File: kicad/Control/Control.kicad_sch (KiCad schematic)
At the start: 66 parts, among them J1 Control Connector, J2 Data Connector, U1 27C64, U10 74LS377, U11 74LS253, U12 74LS253, U13 74LS253, U14 74LS253, U15 74LS253, U16 74LS253, U17 74LS253, U18 74LS257, U19 74LS377, U2 27C64, U20 74LS377, U21 74LS377, U22 74LS138, U23 74LS32, U24 74LS08, U25 74LS86, U26 74LS74, U3 27C64, U4 27C64, U5 27C64, U6 74LS273, U7 74LS377, U8 74LS377, U9 74LS377

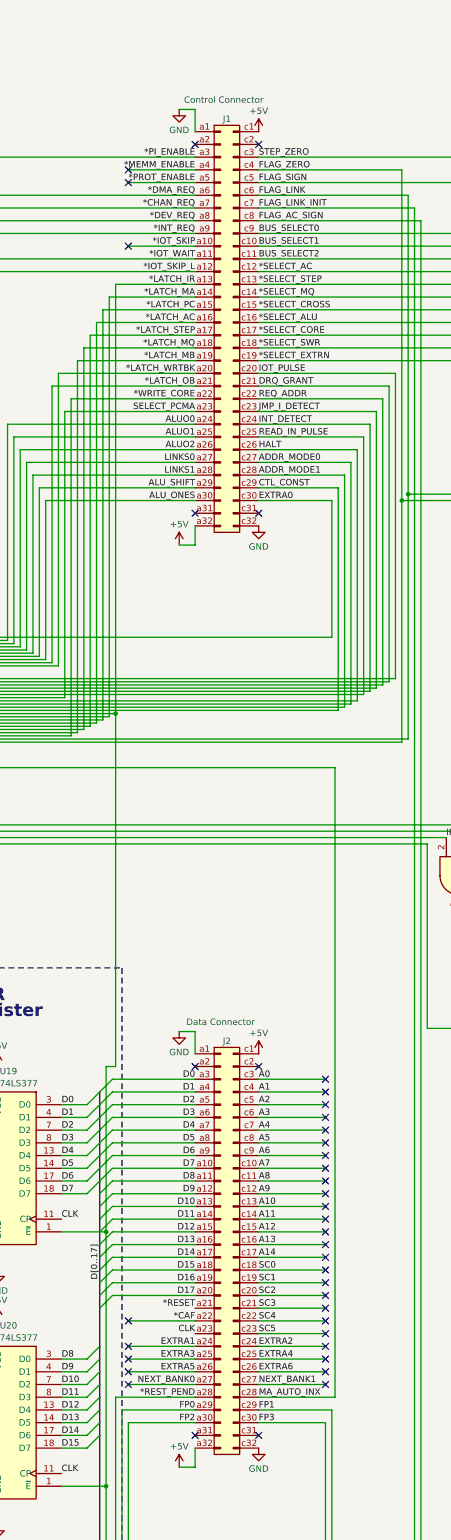
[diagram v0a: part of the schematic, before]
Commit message: Start work on backplane and fix connectors
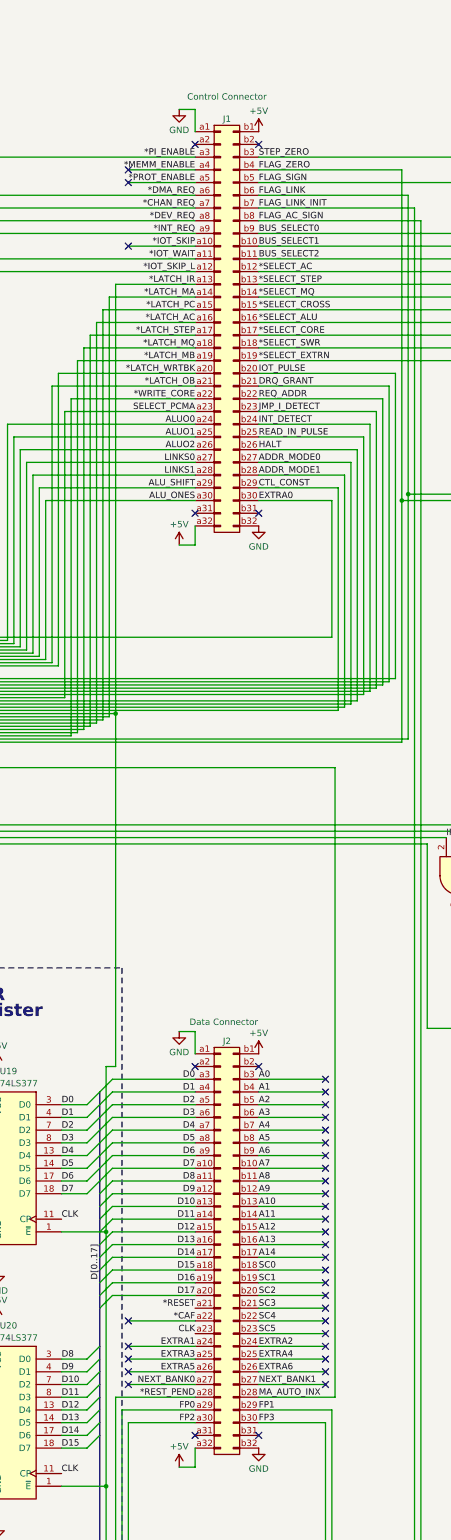
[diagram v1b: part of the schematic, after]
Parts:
- removed J1: Control Connector, symbol Connector:DIN41612_02x32_AC
- removed J2: Data Connector, symbol Connector:DIN41612_02x32_AC
- added J1: Control Connector, Connector_DIN:DIN41612_B_2x32_Male_Horizontal_THT, symbol Connector:DIN41612_02x32_AB
- added J2: Data Connector, Connector_DIN:DIN41612_B_2x32_Male_Horizontal_THT, symbol Connector:DIN41612_02x32_AB
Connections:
- net *CAF: now also J2.a22 (Pin_a22)
- net *CHAN_REQ: now also J1.a7 (Pin_a7)
- net *DEV_REQ: now also J1.a8 (Pin_a8)
- net *DMA_REQ: now also J1.a6 (Pin_a6)
- net *INT_REQ: now also J1.a9 (Pin_a9)
- net *IOT_SKIP: now also J1.a10 (Pin_a10)
- net *IOT_SKIP_L: now also J1.a12 (Pin_a12)
- net *IOT_WAIT: now also J1.a11 (Pin_a11)
- net *LATCH_AC: now also J1.a16 (Pin_a16)
- net *LATCH_IR: now also J1.a13 (Pin_a13)
- net *LATCH_MA: now also J1.a14 (Pin_a14)
- net *LATCH_MB: now also J1.a19 (Pin_a19)
- net *LATCH_MQ: now also J1.a18 (Pin_a18)
- net *LATCH_OB: now also J1.a21 (Pin_a21)
- net *LATCH_PC: now also J1.a15 (Pin_a15)
- net *LATCH_STEP: now also J1.a17 (Pin_a17)
- net *LATCH_WRTBK: now also J1.a20 (Pin_a20)
- net *MEMM_ENABLE: now also J1.a4 (Pin_a4)
- net *PI_ENABLE: now also J1.a3 (Pin_a3)
- net *PROT_ENABLE: now also J1.a5 (Pin_a5)
- net *RESET: now also J2.a21 (Pin_a21)
- net *REST_PEND: now also J2.a28 (Pin_a28)
- net *SELECT_AC: now also J1.b12 (Pin_b12)
- net *SELECT_ALU: now also J1.b16 (Pin_b16)
- net *SELECT_CORE: now also J1.b17 (Pin_b17)
- net *SELECT_CROSS: now also J1.b15 (Pin_b15)
- net *SELECT_EXTRN: now also J1.b19 (Pin_b19)
- net *SELECT_MQ: now also J1.b14 (Pin_b14)
- net *SELECT_STEP: now also J1.b13 (Pin_b13)
- net *SELECT_SWR: now also J1.b18 (Pin_b18)
- net *WRITE_CORE: now also J1.a22 (Pin_a22)
- net +5V: now also J1.a32 (Pin_a32), J1.b1 (Pin_b1), J2.a32 (Pin_a32), J2.b1 (Pin_b1)
- net A0: now also J2.b3 (Pin_b3)
- net A1: now also J2.b4 (Pin_b4)
- net A10: now also J2.b13 (Pin_b13)
- net A11: now also J2.b14 (Pin_b14)
- net A12: now also J2.b15 (Pin_b15)
- net A13: now also J2.b16 (Pin_b16)
- net A14: now also J2.b17 (Pin_b17)
- net A2: now also J2.b5 (Pin_b5)
- net A3: now also J2.b6 (Pin_b6)
- net A4: now also J2.b7 (Pin_b7)
- net A5: now also J2.b8 (Pin_b8)
- net A6: now also J2.b9 (Pin_b9)
- net A7: now also J2.b10 (Pin_b10)
- net A8: now also J2.b11 (Pin_b11)
- net A9: now also J2.b12 (Pin_b12)
- net ADDR_MODE0: now also J1.b27 (Pin_b27)
- net ADDR_MODE1: now also J1.b28 (Pin_b28)
- net ALUO0: now also J1.a24 (Pin_a24)
- net ALUO1: now also J1.a25 (Pin_a25)
- net ALUO2: now also J1.a26 (Pin_a26)
- net ALU_ONES: now also J1.a30 (Pin_a30)
- net ALU_SHIFT: now also J1.a29 (Pin_a29)
- net BUS_SELECT0: now also J1.b9 (Pin_b9)
- net BUS_SELECT1: now also J1.b10 (Pin_b10)
- net BUS_SELECT2: now also J1.b11 (Pin_b11)
- net CLK: now also J2.a23 (Pin_a23)
- net CTL_CONST: now also J1.b29 (Pin_b29)
- net D0: now also J2.a3 (Pin_a3)
- net D1: now also J2.a4 (Pin_a4)
- net D10: now also J2.a13 (Pin_a13)
- net D11: now also J2.a14 (Pin_a14)
- net D12: now also J2.a15 (Pin_a15)
- net D13: now also J2.a16 (Pin_a16)
- net D14: now also J2.a17 (Pin_a17)
- net D15: now also J2.a18 (Pin_a18)
- net D16: now also J2.a19 (Pin_a19)
- net D17: now also J2.a20 (Pin_a20)
- net D2: now also J2.a5 (Pin_a5)
- net D3: now also J2.a6 (Pin_a6)
- net D4: now also J2.a7 (Pin_a7)
- net D5: now also J2.a8 (Pin_a8)
- net D6: now also J2.a9 (Pin_a9)
- net D7: now also J2.a10 (Pin_a10)
- net D8: now also J2.a11 (Pin_a11)
- net D9: now also J2.a12 (Pin_a12)
- net DRQ_GRANT: now also J1.b21 (Pin_b21)
- net EXTRA0: now also J1.b30 (Pin_b30)
- net EXTRA1: now also J2.a24 (Pin_a24)
- net EXTRA2: now also J2.b24 (Pin_b24)
- net EXTRA3: now also J2.a25 (Pin_a25)
- net EXTRA4: now also J2.b25 (Pin_b25)
- net EXTRA5: now also J2.a26 (Pin_a26)
- net EXTRA6: now also J2.b26 (Pin_b26)
- net FLAG_AC_SIGN: now also J1.b8 (Pin_b8)
- net FLAG_LINK: now also J1.b6 (Pin_b6)
- net FLAG_LINK_INIT: now also J1.b7 (Pin_b7)
- net FLAG_SIGN: now also J1.b5 (Pin_b5)
- net FLAG_ZERO: now also J1.b4 (Pin_b4)
- net FP0: now also J2.a29 (Pin_a29)
- net FP1: now also J2.b29 (Pin_b29)
- net FP2: now also J2.a30 (Pin_a30)
- net FP3: now also J2.b30 (Pin_b30)
- net GND: now also J1.a1 (Pin_a1), J1.b32 (Pin_b32), J2.a1 (Pin_a1), J2.b32 (Pin_b32)
- net HALT: now also J1.b26 (Pin_b26)
- net INT_DETECT: now also J1.b24 (Pin_b24)
- net IOT_PULSE: now also J1.b20 (Pin_b20)
- net JMP_I_DETECT: now also J1.b23 (Pin_b23)
- net LINKS0: now also J1.a27 (Pin_a27)
- net LINKS1: now also J1.a28 (Pin_a28)
- net MA_AUTO_INX: now also J2.b28 (Pin_b28)
- net NEXT_BANK0: now also J2.a27 (Pin_a27)
- net NEXT_BANK1: now also J2.b27 (Pin_b27)
- net READ_IN_PULSE: now also J1.b25 (Pin_b25)
- net REQ_ADDR: now also J1.b22 (Pin_b22)
- net SC0: now also J2.b18 (Pin_b18)
- net SC1: now also J2.b19 (Pin_b19)
- net SC2: now also J2.b20 (Pin_b20)
- net SC3: now also J2.b21 (Pin_b21)
- net SC4: now also J2.b22 (Pin_b22)
- net SC5: now also J2.b23 (Pin_b23)
- net SELECT_PCMA: now also J1.a23 (Pin_a23)
- net STEP_ZERO: now also J1.b3 (Pin_b3)
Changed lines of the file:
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@@
     (effects (font (size 1.27 1.27)) (justify right bottom))
   )
-  (symbol (lib_id "Connector:DIN41612_02x32_AC") (at 476.885 273.685 0) (unit 1)
-    (in_bom yes) (on_board yes) (dnp no)
-    (property "Reference" "J2" (at 478.155 233.045 0)
-      (effects (font (size 1.27 1.27)))
-    )
-    (property "Value" "Data Connector" (at 476.885 229.235 0)
-      (effects (font (size 1.27 1.27)))
-    )
-    (property "Footprint" "" (at 476.885 273.685 0)
-      (effects (font (size 1.27 1.27)) hide)
-    )
-    (property "Datasheet" "~" (at 476.885 273.685 0)
-      (effects (font (size 1.27 1.27)) hide)
-    )
-    (pin "a1")
-    (pin "a10")
-    (pin "a11")
-    (pin "a12")
-    (pin "a13")
-    (pin "a14")
-    (pin "a15")
-    (pin "a16")
-    (pin "a17")
-    (pin "a18")
-    (pin "a19")
-    (pin "a2")
-    (pin "a20")
-    (pin "a21")
-    (pin "a22")
-    (pin "a23")
-    (pin "a24")
-    (pin "a25")
-    (pin "a26")
-    (pin "a27")
-    (pin "a28")
-    (pin "a29")
-    (pin "a3")
-    (pin "a30")
-    (pin "a31")
-    (pin "a32")
-    (pin "a4")
-    (pin "a5")
-    (pin "a6")
-    (pin "a7")
-    (pin "a8")
-    (pin "a9")
-    (pin "c1")
-    (pin "c10")
-    (pin "c11")
-    (pin "c12")
-    (pin "c13")
-    (pin "c14")
-    (pin "c15")
-    (pin "c16")
-    (pin "c17")
-    (pin "c18")
-    (pin "c19")
-    (pin "c2")
-    (pin "c20")
-    (pin "c21")
-    (pin "c22")
-    (pin "c23")
-    (pin "c24")
-    (pin "c25")
-    (pin "c26")
-    (pin "c27")
-    (pin "c28")
-    (pin "c29")
-    (pin "c3")
-    (pin "c30")
-    (pin "c31")
-    (pin "c32")
-    (pin "c4")
-    (pin "c5")
-    (pin "c6")
-    (pin "c7")
-    (pin "c8")
-    (pin "c9")
-    (instances
-      (project "Control"
-        (path "/9aceca4c-796d-4c9d-8044-fc5cfdda262d"
-          (reference "J2") (unit 1)
-        )
-      )
-      (project "ALU"
-        (path "/b26dce39-0c19-4808-8ddd-74847f21ad13"
-          (reference "J2") (unit 1)
-        )
-      )
-    )
-  )
   (symbol (lib_id "74xx:74LS74") (at 114.3 385.445 0) (unit 3)
     (in_bom yes) (on_board yes) (dnp no) (fields_autoplaced)
@@
     )
   )
+  (symbol (lib_id "Connector:DIN41612_02x32_AB") (at 476.885 273.685 0) (unit 1)
+    (in_bom yes) (on_board yes) (dnp no)
+    (property "Reference" "J2" (at 478.155 233.045 0)
+      (effects (font (size 1.27 1.27)))
+    )
+    (property "Value" "Data Connector" (at 477.52 229.235 0)
+      (effects (font (size 1.27 1.27)))
+    )
+    (property "Footprint" "Connector_DIN:DIN41612_B_2x32_Male_Horizontal_THT" (at 476.885 273.685 0)
+      (effects (font (size 1.27 1.27)) hide)
+    )
+    (property "Datasheet" "~" (at 476.885 273.685 0)
+      (effects (font (size 1.27 1.27)) hide)
+    )
+    (pin "a1")
+    (pin "a10")
+    (pin "a11")
+    (pin "a12")
+    (pin "a13")
+    (pin "a14")
+    (pin "a15")
+    (pin "a16")
+    (pin "a17")
+    (pin "a18")
+    (pin "a19")
+    (pin "a2")
+    (pin "a20")
+    (pin "a21")
+    (pin "a22")
+    (pin "a23")
+    (pin "a24")
+    (pin "a25")
+    (pin "a26")
+    (pin "a27")
+    (pin "a28")
+    (pin "a29")
+    (pin "a3")
+    (pin "a30")
+    (pin "a31")
+    (pin "a32")
+    (pin "a4")
+    (pin "a5")
+    (pin "a6")
+    (pin "a7")
+    (pin "a8")
+    (pin "a9")
+    (pin "b1")
+    (pin "b10")
+    (pin "b11")
+    (pin "b12")
+    (pin "b13")
+    (pin "b14")
+    (pin "b15")
+    (pin "b16")
+    (pin "b17")
+    (pin "b18")
+    (pin "b19")
+    (pin "b2")
+    (pin "b20")
+    (pin "b21")
+    (pin "b22")
+    (pin "b23")
+    (pin "b24")
+    (pin "b25")
+    (pin "b26")
+    (pin "b27")
+    (pin "b28")
+    (pin "b29")
+    (pin "b3")
+    (pin "b30")
+    (pin "b31")
+    (pin "b32")
+    (pin "b4")
+    (pin "b5")
+    (pin "b6")
+    (pin "b7")
+    (pin "b8")
+    (pin "b9")
+    (instances
+      (project "Control"
+        (path "/9aceca4c-796d-4c9d-8044-fc5cfdda262d"
+          (reference "J2") (unit 1)
+        )
+      )
+      (project "ALU"
+        (path "/b26dce39-0c19-4808-8ddd-74847f21ad13"
+          (reference "J2") (unit 1)
+        )
+      )
+    )
+  )
   (symbol (lib_id "74xx:74LS08") (at 39.37 357.505 0) (unit 4)
     (in_bom yes) (on_board yes) (dnp no) (fields_autoplaced)
@@
     )
   )
-  (symbol (lib_id "Connector:DIN41612_02x32_AC") (at 476.885 89.535 0) (unit 1)
-    (in_bom yes) (on_board yes) (dnp no)
-    (property "Reference" "J1" (at 478.155 48.895 0)
-      (effects (font (size 1.27 1.27)))
-    )
-    (property "Value" "Control Connector" (at 477.52 45.085 0)
-      (effects (font (size 1.27 1.27)))
-    )
-    (property "Footprint" "" (at 476.885 89.535 0)
-      (effects (font (size 1.27 1.27)) hide)
-    )
-    (property "Datasheet" "~" (at 476.885 89.535 0)
-      (effects (font (size 1.27 1.27)) hide)
-    )
-    (pin "a1")
-    (pin "a10")
-    (pin "a11")
-    (pin "a12")
-    (pin "a13")
-    (pin "a14")
-    (pin "a15")
-    (pin "a16")
-    (pin "a17")
-    (pin "a18")
-    (pin "a19")
-    (pin "a2")
-    (pin "a20")
-    (pin "a21")
-    (pin "a22")
-    (pin "a23")
-    (pin "a24")
-    (pin "a25")
-    (pin "a26")
-    (pin "a27")
-    (pin "a28")
-    (pin "a29")
-    (pin "a3")
-    (pin "a30")
-    (pin "a31")
-    (pin "a32")
-    (pin "a4")
-    (pin "a5")
-    (pin "a6")
-    (pin "a7")
-    (pin "a8")
-    (pin "a9")
-    (pin "c1")
-    (pin "c10")
-    (pin "c11")
-    (pin "c12")
-    (pin "c13")
-    (pin "c14")
-    (pin "c15")
-    (pin "c16")
-    (pin "c17")
-    (pin "c18")
-    (pin "c19")
-    (pin "c2")
-    (pin "c20")
-    (pin "c21")
-    (pin "c22")
-    (pin "c23")
-    (pin "c24")
-    (pin "c25")
-    (pin "c26")
-    (pin "c27")
-    (pin "c28")
-    (pin "c29")
-    (pin "c3")
-    (pin "c30")
-    (pin "c31")
-    (pin "c32")
-    (pin "c4")
-    (pin "c5")
-    (pin "c6")
-    (pin "c7")
-    (pin "c8")
-    (pin "c9")
-    (instances
-      (project "Control"
-        (path "/9aceca4c-796d-4c9d-8044-fc5cfdda262d"
-          (reference "J1") (unit 1)
-        )
-      )
-      (project "ALU"
-        (path "/b26dce39-0c19-4808-8ddd-74847f21ad13"
-          (reference "J1") (unit 1)
-        )
-      )
-    )
-  )
   (symbol (lib_id "power:+5V") (at 297.815 293.37 0) (unit 1)
     (in_bom yes) (on_board yes) (dnp no) (fields_autoplaced)
@@
         )
       )
+    )
+  )
+  (symbol (lib_id "Connector:DIN41612_02x32_AB") (at 476.885 89.535 0) (unit 1)
+    (in_bom yes) (on_board yes) (dnp no)
+    (property "Reference" "J1" (at 478.155 48.895 0)
+      (effects (font (size 1.27 1.27)))
+    )
+    (property "Value" "Control Connector" (at 478.155 44.45 0)
+      (effects (font (size 1.27 1.27)))
+    )
+    (property "Footprint" "Connector_DIN:DIN41612_B_2x32_Male_Horizontal_THT" (at 476.885 89.535 0)
+      (effects (font (size 1.27 1.27)) hide)
+    )
+    (property "Datasheet" "~" (at 476.885 89.535 0)
+      (effects (font (size 1.27 1.27)) hide)
+    )
+    (pin "a1")
+    (pin "a10")
+    (pin "a11")
+    (pin "a12")
+    (pin "a13")
+    (pin "a14")
+    (pin "a15")
+    (pin "a16")
+    (pin "a17")
+    (pin "a18")
+    (pin "a19")
+    (pin "a2")
+    (pin "a20")
+    (pin "a21")
+    (pin "a22")
+    (pin "a23")
+    (pin "a24")
+    (pin "a25")
+    (pin "a26")
+    (pin "a27")
+    (pin "a28")
+    (pin "a29")
+    (pin "a3")
+    (pin "a30")
+    (pin "a31")
+    (pin "a32")
+    (pin "a4")
+    (pin "a5")
+    (pin "a6")
+    (pin "a7")
+    (pin "a8")
+    (pin "a9")
+    (pin "b1")
+    (pin "b10")
+    (pin "b11")
+    (pin "b12")
+    (pin "b13")
+    (pin "b14")
+    (pin "b15")
+    (pin "b16")
+    (pin "b17")
+    (pin "b18")
+    (pin "b19")
+    (pin "b2")
+    (pin "b20")
+    (pin "b21")
+    (pin "b22")
+    (pin "b23")
+    (pin "b24")
+    (pin "b25")
+    (pin "b26")
+    (pin "b27")
+    (pin "b28")
+    (pin "b29")
+    (pin "b3")
+    (pin "b30")
+    (pin "b31")
+    (pin "b32")
+    (pin "b4")
+    (pin "b5")
+    (pin "b6")
+    (pin "b7")
+    (pin "b8")
+    (pin "b9")
+    (instances
+      (project "Control"
+        (path "/9aceca4c-796d-4c9d-8044-fc5cfdda262d"
+          (reference "J1") (unit 1)
+        )
+      )
+      (project "ALU"
+        (path "/b26dce39-0c19-4808-8ddd-74847f21ad13"
+          (reference "J1") (unit 1)
+        )
+      )

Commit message: Update backplane pin logic levels
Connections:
- net DRQ_GRANT renamed *DRQ_GRANT
- net INT_DETECT renamed *INT_DETECT
- net IOT_PULSE renamed *IOT_PULSE
- net JMP_I_DETECT renamed *JMP_I_DETECT
- net READ_IN_PULSE renamed *READ_IN_PULSE
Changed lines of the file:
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@@
     (effects (font (size 1.27 1.27)) (justify right bottom))
   )
-  (label "INT_DETECT" (at 257.175 124.46 0) (fields_autoplaced)
+  (label "*INT_DETECT" (at 257.175 124.46 0) (fields_autoplaced)
     (effects (font (size 1.27 1.27)) (justify left bottom))
   )
@@
     (effects (font (size 1.27 1.27)) (justify left bottom))
   )
-  (label "JMP_I_DETECT" (at 484.505 107.315 0) (fields_autoplaced)
+  (label "*JMP_I_DETECT" (at 484.505 107.315 0) (fields_autoplaced)
     (effects (font (size 1.27 1.27)) (justify left bottom))
   )
@@
     (effects (font (size 1.27 1.27)) (justify right bottom))
   )
-  (label "IOT_PULSE" (at 257.175 114.3 0) (fields_autoplaced)
+  (label "*IOT_PULSE" (at 257.175 114.3 0) (fields_autoplaced)
     (effects (font (size 1.27 1.27)) (justify left bottom))
   )
@@
     (effects (font (size 1.27 1.27)) (justify right bottom))
   )
-  (label "IOT_PULSE" (at 484.505 99.695 0) (fields_autoplaced)
+  (label "*IOT_PULSE" (at 484.505 99.695 0) (fields_autoplaced)
     (effects (font (size 1.27 1.27)) (justify left bottom))
   )
@@
     (effects (font (size 1.27 1.27)) (justify right bottom))
   )
-  (label "JMP_I_DETECT" (at 257.175 121.92 0) (fields_autoplaced)
+  (label "*JMP_I_DETECT" (at 257.175 121.92 0) (fields_autoplaced)
     (effects (font (size 1.27 1.27)) (justify left bottom))
   )
@@
     (effects (font (size 1.27 1.27)) (justify left bottom))
   )
-  (label "DRQ_GRANT" (at 257.175 116.84 0) (fields_autoplaced)
+  (label "*DRQ_GRANT" (at 257.175 116.84 0) (fields_autoplaced)
     (effects (font (size 1.27 1.27)) (justify left bottom))
   )
@@
     (effects (font (size 1.27 1.27)) (justify right bottom))
   )
-  (label "READ_IN_PULSE" (at 257.175 127 0) (fields_autoplaced)
+  (label "*READ_IN_PULSE" (at 257.175 127 0) (fields_autoplaced)
     (effects (font (size 1.27 1.27)) (justify left bottom))
   )
@@
     (effects (font (size 1.27 1.27)) (justify right bottom))
   )
-  (label "READ_IN_PULSE" (at 484.505 112.395 0) (fields_autoplaced)
+  (label "*READ_IN_PULSE" (at 484.505 112.395 0) (fields_autoplaced)
     (effects (font (size 1.27 1.27)) (justify left bottom))
   )
@@
     (effects (font (size 1.27 1.27)) (justify left bottom))
   )
-  (label "DRQ_GRANT" (at 484.505 102.235 0) (fields_autoplaced)
+  (label "*DRQ_GRANT" (at 484.505 102.235 0) (fields_autoplaced)
     (effects (font (size 1.27 1.27)) (justify left bottom))
   )
@@
     (effects (font (size 1.27 1.27)) (justify right bottom))
   )
-  (label "INT_DETECT" (at 484.505 109.855 0) (fields_autoplaced)
-    (effects (font (size 1.27 1.27)) (justify left bottom))
-  )
+  (label "*INT_DETECT" (at 484.505 109.855 0) (fields_autoplaced)
+    (effects (font (size 1.27 1.27)) (justify left bottom))
+  )

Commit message: The great PCB layout-athon
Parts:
- added J3: State Debug, Connector_IDC:IDC-Header_2x06_P2.54mm_Horizontal, symbol Connector_Generic:Conn_02x06_Counter_Clockwise
- C1, C10, C11, C12, C13, C14, C15, C16, C17, C18, C19, C2, C20, C21, C22, C23, C24, C25, C26, C3, C4, C5, C6, C7, C8, C9: footprint (none) -> Capacitor_THT:C_Disc_D5.0mm_W2.5mm_P5.00mm
- R1, R10, R11, R2, R3, R4, R5, R6, R7, R8, R9: footprint (none) -> Resistor_THT:R_Axial_DIN0207_L6.3mm_D2.5mm_P7.62mm_Horizontal
- U10, U19, U20, U21, U6, U7, U8, U9: footprint (none) -> Package_DIP:DIP-20_W7.62mm
- U11, U12, U13, U14, U15, U16, U17, U18, U22: footprint (none) -> Package_DIP:DIP-16_W7.62mm
- U23, U24, U25, U26: footprint (none) -> Package_DIP:DIP-14_W7.62mm
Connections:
- net *RESET: now also J3.8 (Pin_8)
- net +5V: now also J3.1 (Pin_1)
- net CLK: now also J3.9 (Pin_9)
- net GND: now also J3.7 (Pin_7)
- net ST0: now also J3.2 (Pin_2)
- net ST11: now also J3.10 (Pin_10)
- net ST12: now also J3.11 (Pin_11)
- net STEP1: now also J3.3 (Pin_3)
- net STEP2: now also J3.4 (Pin_4)
- net STEP3: now also J3.5 (Pin_5)
- net STEP4: now also J3.6 (Pin_6)
- net STEP5: now also J3.12 (Pin_12)
